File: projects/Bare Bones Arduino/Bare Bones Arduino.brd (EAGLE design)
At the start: 76.2 x 68.6 mm, 14 parts, among them IC1 AVR-MEGA8-P

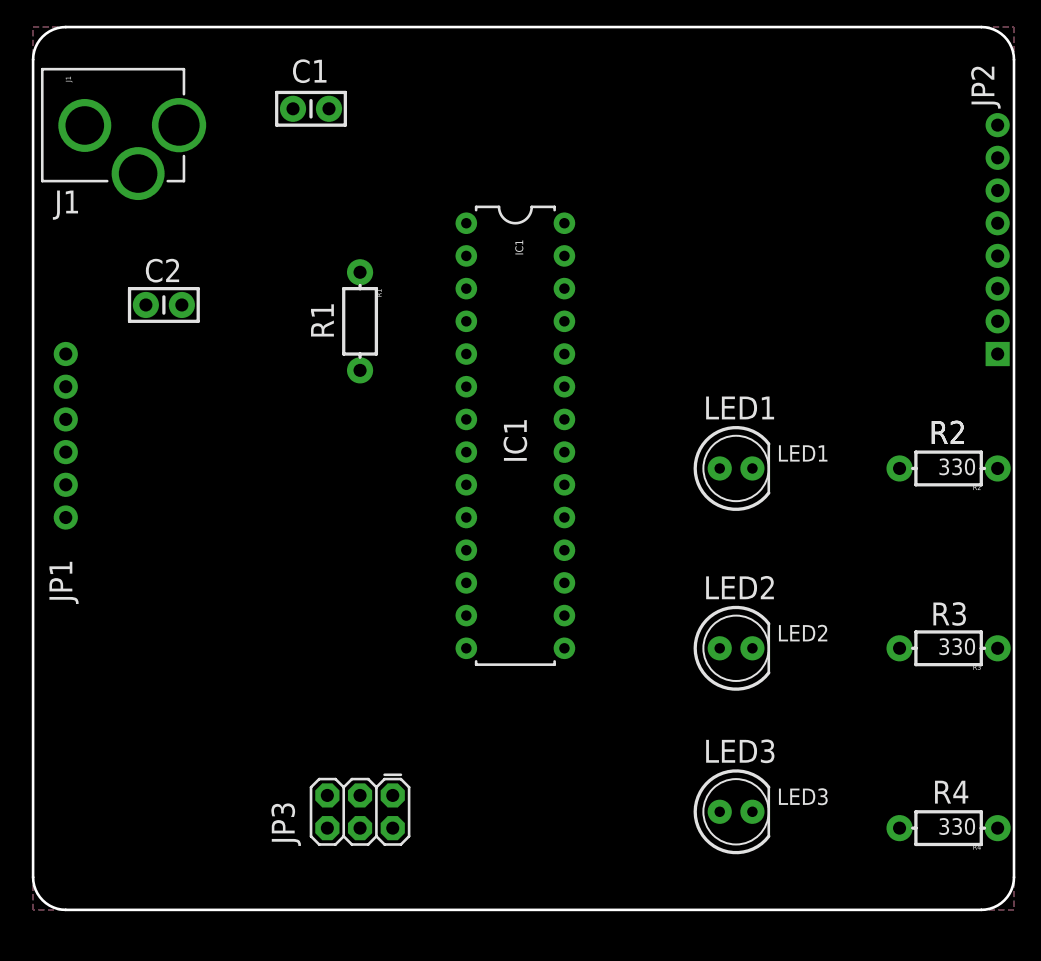
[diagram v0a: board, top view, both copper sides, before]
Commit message: Updating Eagle files, adding documentation
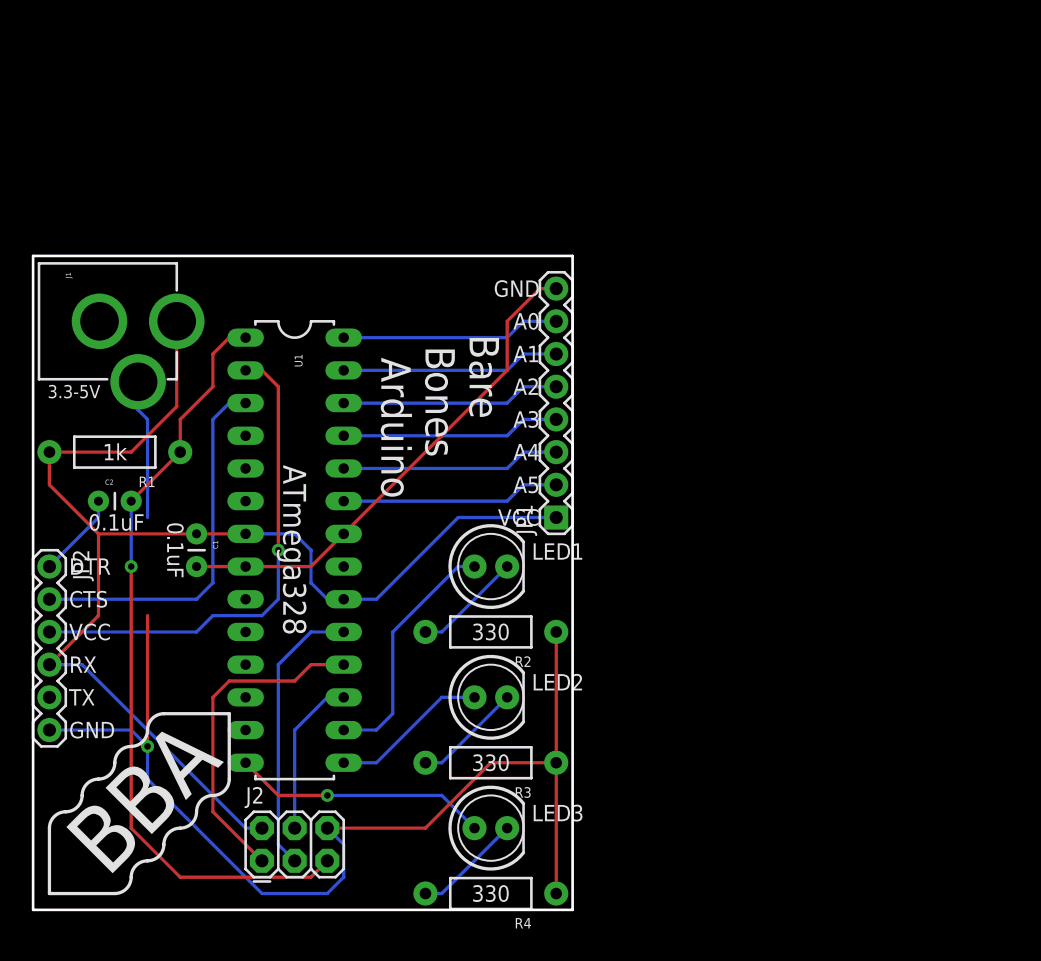
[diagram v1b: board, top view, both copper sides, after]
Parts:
- removed IC1: AVR-MEGA8-P, Testing:DIL28-3-SIMON
- removed JP3: (no value), SparkFun:2X3
- added FRAME1: FRAME-LETTER, SparkFun-Aesthetics:CREATIVE_COMMONS
- added J2: AVR_SPI_PRG_6PTH, SparkFun-Connectors:2X3
- added U1: ATMEGA328P_PDIP, SparkFun-DigitalIC:DIL28-3
- C1, C2: value 0.1uF -> (none); device SparkFun:CAP-PTH-SMALL-KIT -> SparkFun-Capacitors:CAP-PTH-SMALL
- J1: value (none) -> POWER_JACKPTH; device SparkFun:POWER_JACK_PTH_LOCK -> SparkFun-Connectors:POWER_JACK_PTH
- JP1: value Serial -> (none); device unclepetes:1X06-NOSILK -> SparkFun-Connectors:1X08
- JP2: device unclepetes:1X08NOSILK -> SparkFun-Connectors:1X06
- LED1, LED2, LED3: device SparkFun:LED5MM -> SparkFun-LED:LED5MM
- R1: value 10K -> (none); device SparkFun:AXIAL-0.3-KIT -> SparkFun-Resistors:AXIAL-0.4
- R2, R3, R4: value 330 -> (none); device SparkFun:AXIAL-0.3-KIT -> SparkFun-Resistors:AXIAL-0.4
- moved JP2 75.5 mm to (1.27, 26.7), flipped to the top, turned to 270 degrees
- moved JP1 40.2 mm to (40.6, 30.5), flipped to the top, turned to 90 degrees
- moved R2 37.8 mm to (35.6, 21.6)
- moved R3 36.7 mm to (35.6, 11.4)
- moved R4 35.9 mm to (35.6, 1.27)
- moved C1 34.5 mm to (12.7, 29.2), turned to 270 degrees
- moved R1 21.6 mm to (6.35, 35.6), turned to 180 degrees
- moved LED1 20.5 mm to (35.6, 26.7)
- moved LED2 19.4 mm to (35.6, 16.5)
- moved LED3 19.1 mm to (35.6, 6.35)
- moved C2 15.7 mm to (5.08, 31.8)
- moved J1 15.2 mm to (-2.54, 45.7)
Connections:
- removed net 3.3V: C1.2, IC1.20, IC1.21, IC1.7, J1.PWR, JP2.2, JP3.2, R1.P$2
- removed net A0: IC1.23, JP2.3
- removed net A1: IC1.24, JP2.4
- removed net A2: IC1.25, JP2.5
- removed net A3: IC1.26, JP2.6
- removed net A4: IC1.27, JP2.7
- removed net A5: IC1.28, JP2.8
- removed net D10: IC1.16, LED1.A
- removed net D2: IC1.4
- removed net D3: IC1.5
- removed net D4: IC1.6
- removed net D5: IC1.11
- removed net D6: IC1.12
- removed net D7: IC1.13
- removed net D8: IC1.14, LED3.A
- removed net D9: IC1.15, LED2.A
- removed net RX-I: IC1.2, JP1.3
- removed net TX-O: IC1.3, JP1.2
- new net CTS: JP2.5
- new net N$1: LED1.A, U1.16
- new net N$10: JP1.5, U1.26
- new net N$11: JP1.6, U1.27
- new net N$12: JP1.7, U1.28
- new net N$2: LED2.A, U1.15
- new net N$3: LED3.A, U1.14
- new net N$7: JP1.2, U1.23
- new net N$8: JP1.3, U1.24
- new net N$9: JP1.4, U1.25
- new net RX: JP2.3, U1.2
- new net TX: JP2.2, U1.3
- new net VCC: C1.1, J1.PWR, J2.2, JP1.1, JP2.4, R1.P$2, U1.20, U1.7
- net DTR: now also JP2.1; no longer JP1.1
- net GND: now also C1.2, J2.6, JP1.8, JP2.6, U1.22, U1.8; no longer C1.1, IC1.22, IC1.8, JP1.5, JP1.6, JP2.1, JP3.6
- net MISO: now also J2.1, U1.18; no longer IC1.18, JP3.1
- net MOSI: now also J2.4, U1.17; no longer IC1.17, JP3.4
- net RESET: now also J2.5, U1.1; no longer IC1.1, JP3.5
- net SCK: now also J2.3, U1.19; no longer IC1.19, JP3.3
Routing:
- net GND: track 0.00 -> 136.5 mm, vias 0 -> 1
- net VCC: track 0.00 -> 101.2 mm
- net RESET: track 0.00 -> 59.9 mm, vias 0 -> 1
- net RX: track 0.00 -> 38.4 mm, vias 0 -> 1
- net TX: track 0.00 -> 29.0 mm
- net MISO: track 0.00 -> 25.5 mm
- net SCK: track 0.00 -> 21.9 mm
- net N$3: track 0.00 -> 19.9 mm, vias 0 -> 1
- net N$1: track 0.00 -> 19.1 mm
- net N$9: track 0.00 -> 17.0 mm
- net N$8: track 0.00 -> 17.0 mm
- net N$7: track 0.00 -> 17.0 mm
- net N$11: track 0.00 -> 17.0 mm
- net N$10: track 0.00 -> 17.0 mm
- net N$12: track 0.00 -> 17.0 mm
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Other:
- board size 76.2 x 68.6 mm -> 41.9 x 50.8 mm
- board text added: "0.1uF"
- board text added: "1k"
- board text added: "3.3-5V"
- board text added: "330"
- board text added: "A0"
- board text added: "A1"
- board text added: "A2"
- board text added: "A3"
- board text added: "A4"
- board text added: "A5"
- board text added: "ATmega328"
- board text added: "BBA"
- board text added: "Bare Bones Arduino"
- board text added: "CTS"
- board text added: "DTR"
- board text added: "GND"
- board text added: "RX"
- board text added: "TX"
- board text added: "VCC"
- board text removed: "All thru hole components make joint on bottom"
- board text removed: "All thru hole components make joint on top side"
- board text removed: "C1"
- board text removed: "C2"
- board text removed: "IC1"
- board text removed: "J1"
- board text removed: "JP1"
- board text removed: "JP2"
- board text removed: "JP3"
- board text removed: "LED1"
- board text removed: "LED2"
- board text removed: "LED3"
- board text removed: "R1"
- board text removed: "R2"
- board text removed: "R3"
- board text removed: "R4"
